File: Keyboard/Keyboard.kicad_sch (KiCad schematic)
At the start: 72 parts, among them SW1 SW_TOUCHE, SW10 SW_TOUCHE, SW11 SW_TOUCHE, SW12 SW_TOUCHE, SW13 SW_TOUCHE, SW14 SW_TOUCHE, SW15 SW_TOUCHE, SW16 SW_TOUCHE, SW17 SW_TOUCHE, SW18 SW_TOUCHE, SW19 SW_TOUCHE, SW2 SW_TOUCHE, SW20 SW_TOUCHE, SW21 SW_TOUCHE, SW22 SW_TOUCHE, SW23 SW_TOUCHE, SW24 SW_TOUCHE, SW25 SW_TOUCHE, SW26 SW_TOUCHE, SW27 SW_TOUCHE, SW28 SW_TOUCHE, SW29 SW_TOUCHE, SW3 SW_TOUCHE, SW30 SW_TOUCHE, SW31 SW_TOUCHE, SW32 SW_TOUCHE, SW33 SW_TOUCHE, SW34 SW_TOUCHE, SW35 SW_TOUCHE, SW36 SW_TOUCHE, SW4 SW_TOUCHE, SW5 SW_TOUCHE, SW6 SW_TOUCHE, SW7 SW_TOUCHE, SW8 SW_TOUCHE, SW9 SW_TOUCHE

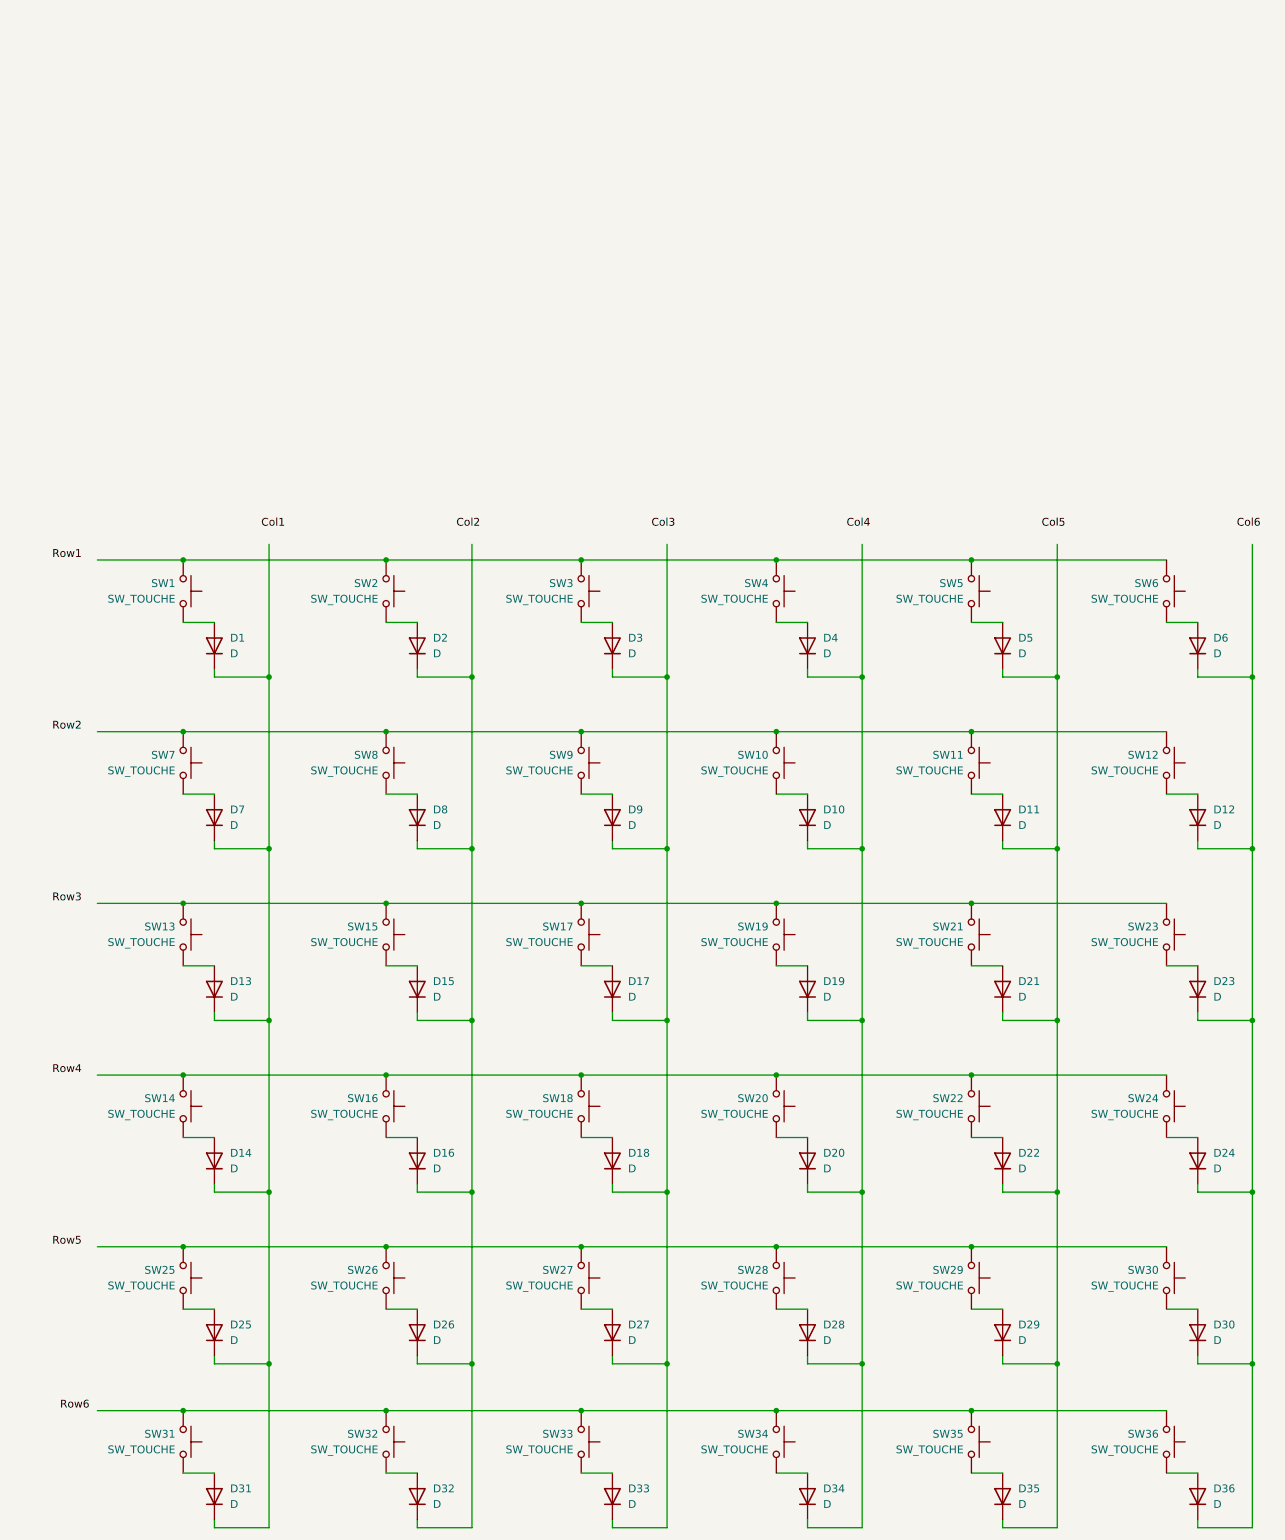
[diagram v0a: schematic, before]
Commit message: add: demux 1x6 schematics
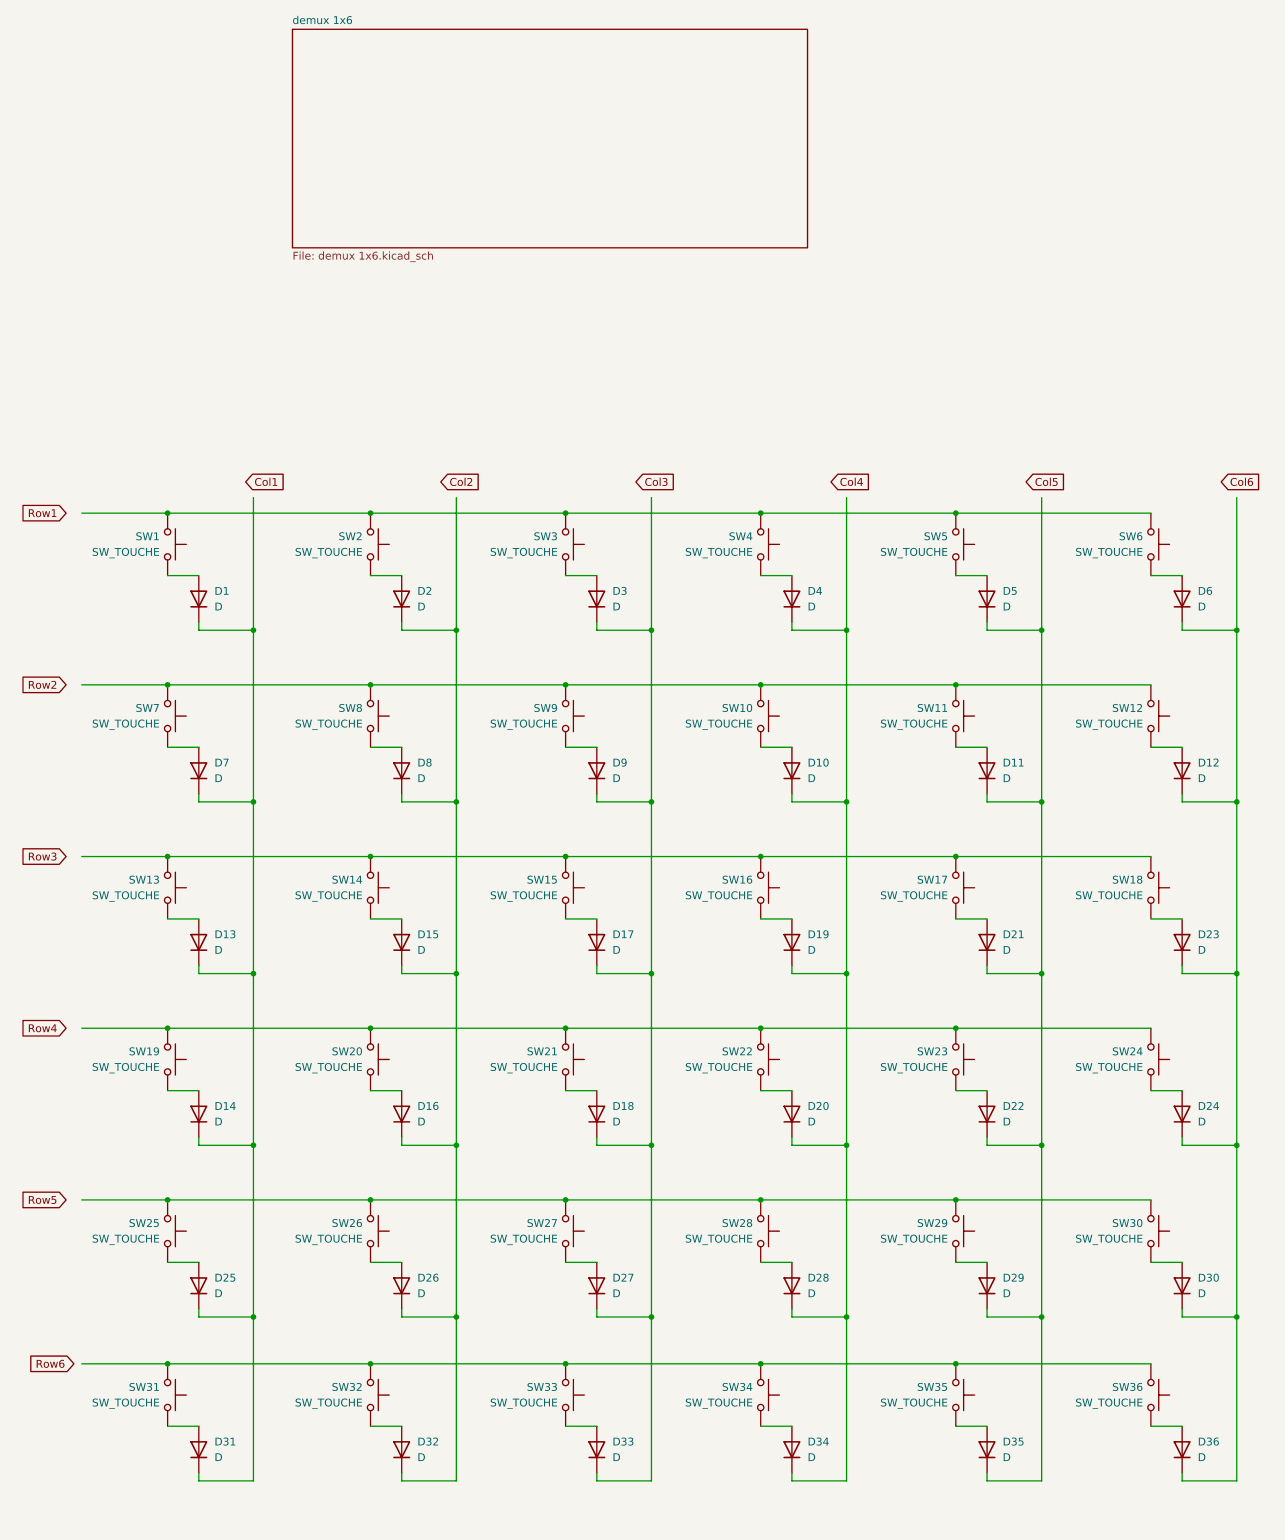
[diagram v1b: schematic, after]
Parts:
- SW1, SW10, SW11, SW12, SW13, SW14, SW15, SW16, SW17, SW18, SW19, SW2, SW20, SW21, SW22, SW23, SW24, SW25, SW26, SW27, SW28, SW29, SW3, SW30, SW31, SW32, SW33, SW34, SW35, SW36, SW4, SW5, SW6, SW7, SW8, SW9: footprint (none) -> Button_Switch_Keyboard:SW_Cherry_MX_1.00u_PCB
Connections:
- net at D15.2 (A): now also SW14.2; no longer SW15.2
- net at D21.2 (A): now also SW17.2; no longer SW21.2
- net at SW14.1, SW16.1, SW18.1: now also SW13.1, SW15.1, SW17.1; no longer SW20.1, SW22.1, SW24.1
- net at D18.2 (A): now also SW21.2; no longer SW18.2
- net at SW22.2: now also D20.2 (A); no longer D22.2 (A)
- net at SW20.2: now also D16.2 (A); no longer D20.2 (A)
- net at SW19.1, SW21.1, SW23.1: now also SW20.1, SW22.1, SW24.1; no longer SW13.1, SW15.1, SW17.1
- net at D14.2 (A): now also SW19.2; no longer SW14.2
- net at D17.2 (A): now also SW15.2; no longer SW17.2
- net at SW23.2: now also D22.2 (A); no longer D23.2 (A)
- net at D19.2 (A): now also SW16.2; no longer SW19.2
- new net: D23.2 (A), SW18.2
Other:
- added sheet demux 1x6 (demux 1x6.kicad_sch)
- moved on the sheet: D1, D10, D11, D12, D13, D14, D15, D16, D17, D18, D19, D2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
